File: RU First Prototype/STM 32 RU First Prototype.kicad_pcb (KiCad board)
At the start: 4 copper layers, 45 x 81.5 mm, 98 parts, among them J1 Conn_01x02, J10 Conn_01x02_Pin, J11 Conn_01x02_Pin, J12 1776113-2, J2 USB_C_Receptacle, J3 Conn_01x02_Pin, J4 Conn_01x04, J5 Conn_01x02_Pin, J7 1776113-2, J9 Conn_01x02_Pin, Q1 SISA96DN-T1, Q3 SISA96DN-T1, SW1 SW_SPDT, U1 STM32F412RGTx, U2 AMS1117-3.3, U3 MS5611, U4 KX134-1211, U5 W25Q16JVSS, U6 TCAN330, U7 TCAN330, Y1 Crystal_8Mhz

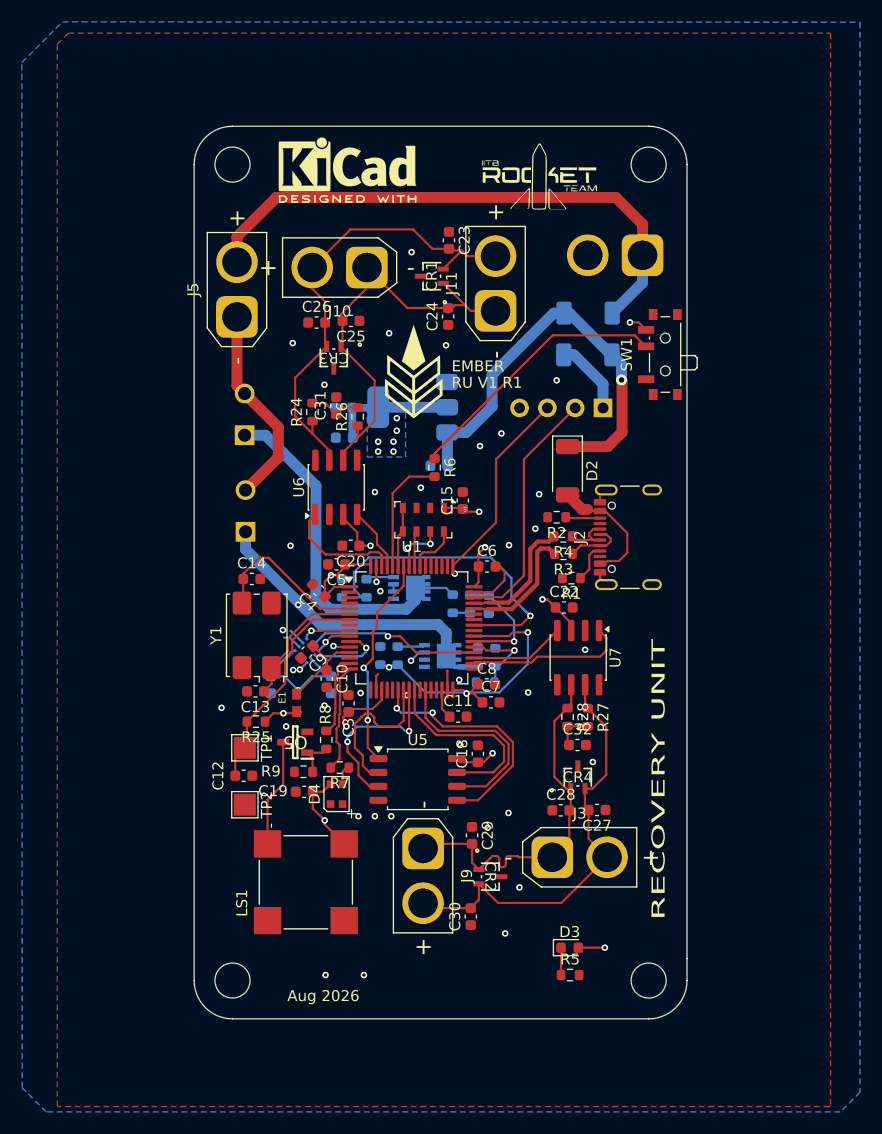
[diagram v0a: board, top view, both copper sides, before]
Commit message: changed CAN xt30 to jst 2.5
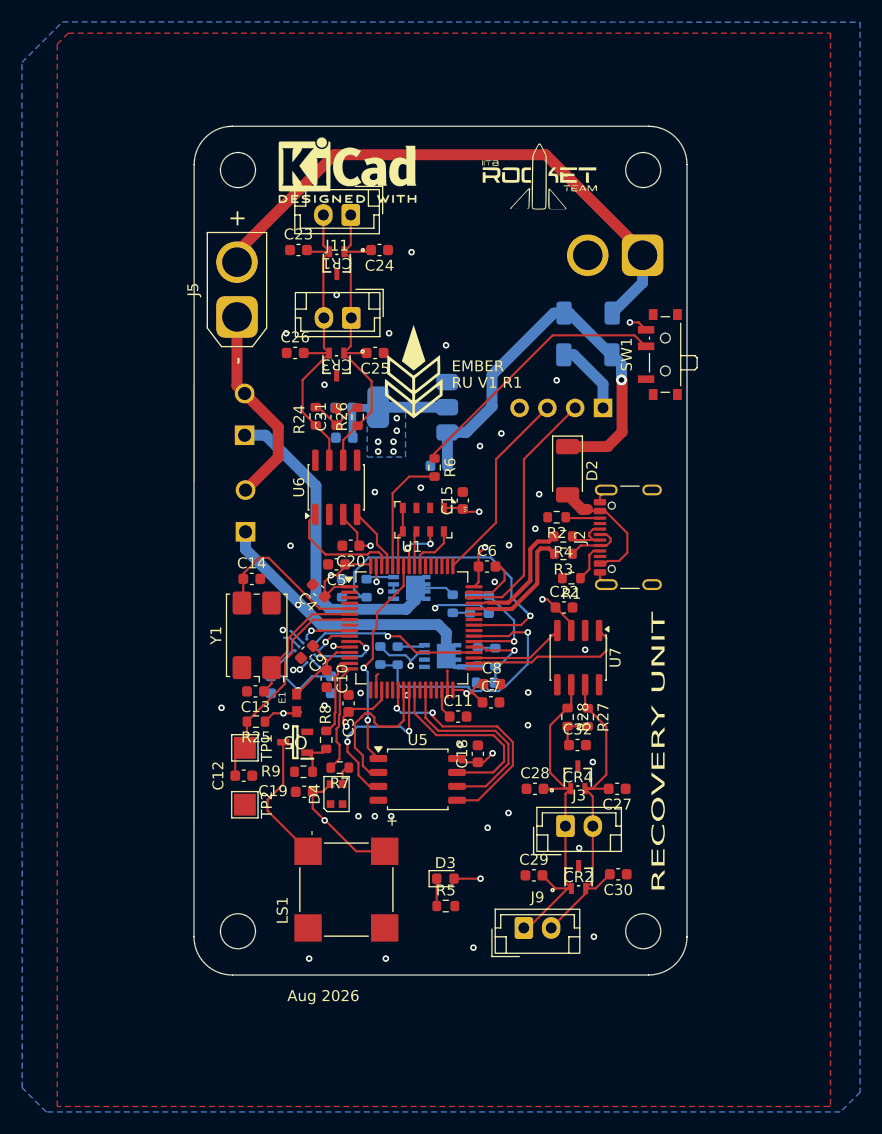
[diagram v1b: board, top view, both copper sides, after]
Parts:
- J10, J11, J3, J9: footprint Connector_AMASS:AMASS_XT30U-M_1x02_P5.0mm_Vertical -> Connector_JST:JST_EH_B2B-EH-A_1x02_P2.50mm_Vertical
- moved J11 15.9 mm to (115.8, 62.1), turned to 180 degrees
- moved C30 14.0 mm to (140.2, 122.3), turned to 180 degrees
- moved C23 13.8 mm to (111.0, 65.3), turned to 0 degrees
- moved D3 13.0 mm to (124.4, 122.7)
- moved R5 13.0 mm to (124.5, 125.2)
- moved J9 11.7 mm to (131.6, 127.2), turned to 0 degrees
- moved CR1 8.75 mm to (114.5, 66.5), turned to 180 degrees
- moved C24 8.72 mm to (118.4, 65.3), turned to 180 degrees
- moved CR2 8.06 mm to (136.6, 122.5), turned to 0 degrees
- moved C29 6.73 mm to (132.5, 122.4), turned to 0 degrees
- moved J10 4.82 mm to (115.8, 71.5)
- moved REF** 4.53 mm to (105.5, 127.5)
- moved REF** 4.53 mm to (142.5, 127.5)
- moved LS1 3.76 mm to (115.4, 123.7)
- moved C25 3.67 mm to (118.0, 74.7)
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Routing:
- net /CAN_H: track 43.7 -> 29.6 mm
- net GND: track 20.8 -> 30.4 mm, vias 44 -> 46
- net /CAN_L: track 39.2 -> 30.0 mm
- net /CAN_H2: track 40.1 -> 31.1 mm
- net +3V3: track 79.5 -> 83.2 mm
- net Net-(Q5-D): track 9.88 -> 12.1 mm
- net /CAN_L2: track 34.4 -> 32.4 mm
- net /Drogue: track 23.7 -> 25.2 mm
- net /V_2S: track 52.2 -> 53.1 mm
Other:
- board size 45 x 81.5 mm -> 45 x 77.5 mm

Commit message: edge cuts adjustments
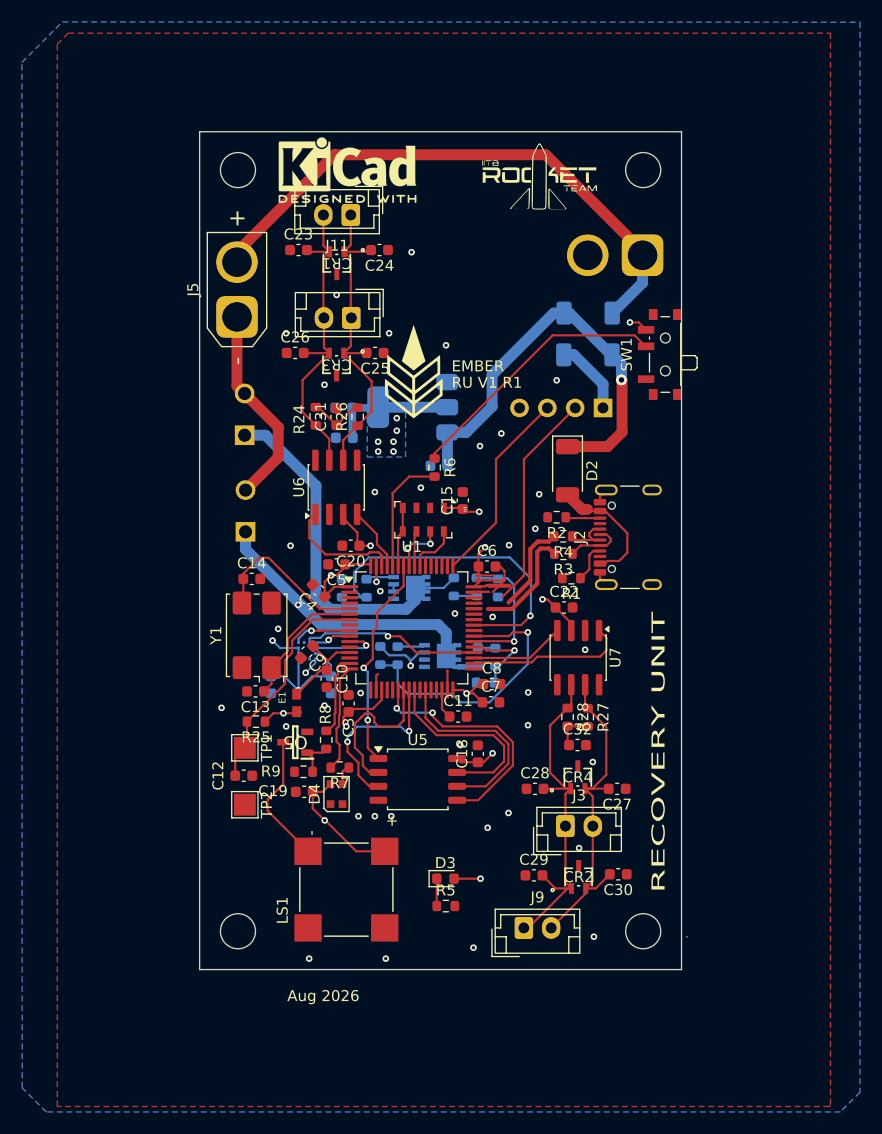
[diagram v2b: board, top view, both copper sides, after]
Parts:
- moved R20 1.74 mm to (129.2, 96.2)
- moved R19 1.68 mm to (127.3, 96.1)
- moved R18 1.54 mm to (125.2, 96.1)
- turned U4 to 180 degrees
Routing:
- net GND: track 30.4 -> 25.4 mm, vias 46 -> 44
- net /PC7: track 10.6 -> 12.7 mm
- net /D-: track 11.5 -> 10.3 mm
- net /KX_CS: track 4.43 -> 5.33 mm
- net /KX_SDI: track 7.34 -> 6.80 mm
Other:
- board size 45 x 77.5 mm -> 44.5 x 76.5 mm

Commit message: Final touch done from my side
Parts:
- removed the G*** at (121.5, 76.5)
- added G***: LOGO, RT_Graphics:project_logo_huge.kicad_sym, F.Cu at (110.0, 104.2)
- C15, U3: moved to B.Cu
- C16, C17, J1, U4: moved to F.Cu
- moved C15 25.4 mm to (109.3, 107.3), turned to -90 degrees
- moved C17 21.4 mm to (121.2, 87.8), turned to 90 degrees
- moved C16 18.8 mm to (123.9, 89.0), turned to 90 degrees
- moved U3 16.8 mm to (111.7, 102.9), turned to 0 degrees
- moved U4 14.8 mm to (121.5, 90.7)
- moved G*** 13.4 mm to (126.3, 70.6)
- moved REF** 10.5 mm to (126.0, 59.0)
- moved J1 9.70 mm to (135.5, 59.0), turned to -90 degrees
- moved TP2 2.19 mm to (106.1, 118.1)
- moved C12 1.95 mm to (106.1, 115.2)
- moved TP1 1.26 mm to (106.2, 112.0)
- moved REF** 0.71 mm to (106.0, 127.0)
- moved C19 0.70 mm to (111.5, 115.5)
- moved J5 0.59 mm to (106.0, 71.4)
- moved REF** 0.57 mm to (105.9, 58.4)
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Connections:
- U1 pad 10: /KX_SDO -> /ALT_SDO
- U1 pad 11: /KX_SDI -> /ALT_SDI
- U1 pad 36: /KX_SCK -> /ALT_SCLK
- U1 pad 55: /ALT_SCLK -> /KX_SCK
- U1 pad 56: /ALT_SDO -> /KX_SDO
- U1 pad 57: /ALT_SDI -> /KX_SDI
- U1 pad 59: /ALT_CS -> /KX_CS
- U1 pad 9: /KX_CS -> /ALT_CS
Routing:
- net /KX_SCK: track 16.3 -> 2.89 mm, vias 1 -> 0
- net /ALT_SCLK: track 4.66 -> 16.7 mm, vias 0 -> 1
- net +3V3: track 83.7 -> 77.3 mm
- net /ALT_SDI: track 5.04 -> 10.7 mm, vias 2 -> 1
- net GND: track 25.4 -> 29.5 mm, vias 44 -> 48
- net /V_2S: track 53.1 -> 49.5 mm
- net /ALT_CS: track 5.45 -> 7.21 mm, vias 0 -> 1
- net /KX_SDO: track 3.45 -> 5.20 mm, vias 1 -> 2
- net /BOOT0: track 11.1 -> 12.5 mm
- net /D-: track 10.3 -> 11.5 mm
- net /NRST: track 21.4 -> 22.4 mm
- net /KX_CS: track 5.33 -> 4.45 mm, vias 1 -> 0
- net /ALT_SDO: track 3.20 -> 3.99 mm, vias 0 -> 1
- net /Main: track 31.7 -> 31.0 mm
- net /V_USB: track 12.0 -> 11.5 mm
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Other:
- outline, holes or cut-outs redrawn
- board text added: "Every av component has to have a cursed looking prototype - The person who has this r*t**ded idead called TSMBAS"
- board text added: "REV 1"
- board text added: "RU V1R1"
- board text removed: "EMBER"
- board text removed: "RU V1 R1"

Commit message: Fixed schematic and some routing, flash routing left
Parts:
- moved C15 16.9 mm to (125.3, 112.8), turned to 0 degrees
- moved U3 11.8 mm to (120.9, 110.4), turned to 90 degrees
- moved E1 1.73 mm to (111.1, 104.9)
- moved R7 1.41 mm to (113.6, 113.3)
- moved C19 1.39 mm to (110.2, 115.8)
- moved C10 1.37 mm to (112.8, 103.3)
- moved C9 1.30 mm to (112.1, 100.7)
- moved R9 1.26 mm to (110.2, 113.1)
- moved D4 1.24 mm to (113.7, 115.9)
- moved Q5 0.90 mm to (109.8, 110.3)
- moved R25 0.80 mm to (106.8, 107.6)
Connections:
- U1 pad 1: +3V3 -> unconnected-(U1-VBAT-Pad1)
- U1 pad 10: /ALT_SDO -> unconnected-(U1-PC2-Pad10)
- U1 pad 11: /ALT_SDI -> unconnected-(U1-PC3-Pad11)
- U1 pad 14: unconnected-(U1-PA0-Pad14) -> /Buzzer_G
- U1 pad 15: /Buzzer_G -> /FLASH_IO3
- U1 pad 20: unconnected-(U1-PA4-Pad20) -> /ALT_CS
- U1 pad 21: unconnected-(U1-PA5-Pad21) -> /ALT_SCLK
- U1 pad 22: /FLASH_IO0 -> /ALT_SDI
- U1 pad 23: /FLASH_IO1 -> /ALT_SDO
- U1 pad 24: /FLASH_IO2 -> unconnected-(U1-PC4-Pad24)
- U1 pad 25: /FLASH_IO3 -> unconnected-(U1-PC5-Pad25)
- U1 pad 33: unconnected-(U1-PB12-Pad33) -> /CAN_RX2
- U1 pad 35: /CAN_RX2 -> unconnected-(U1-PB14-Pad35)
- U1 pad 36: /ALT_SCLK -> unconnected-(U1-PB15-Pad36)
- U1 pad 39: /Drogue -> /FLASH_IO2
- U1 pad 40: unconnected-(U1-PC9-Pad40) -> /FLASH_IO0
- U1 pad 42: unconnected-(U1-PA9-Pad42) -> /Drogue
- U1 pad 51: unconnected-(U1-PC10-Pad51) -> /FLASH_IO1
- U1 pad 52: unconnected-(U1-PC11-Pad52) -> /KX_SDI
- U1 pad 53: unconnected-(U1-PC12-Pad53) -> /KX_SDO
- U1 pad 56: /KX_SDO -> unconnected-(U1-PB4-Pad56)
- U1 pad 57: /KX_SDI -> unconnected-(U1-PB5-Pad57)
- U1 pad 9: /ALT_CS -> unconnected-(U1-PC1-Pad9)
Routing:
- net /FLASH_IO3: track 17.7 -> 0.00 mm
- net /FLASH_IO1: track 14.5 -> 27.0 mm, vias 0 -> 2
- net /FLASH_IO2: track 16.3 -> 27.8 mm
- net GND: track 29.5 -> 18.6 mm, vias 48 -> 43
- net /ALT_SCLK: track 16.7 -> 8.86 mm
- net /ALT_SDI: track 10.7 -> 4.46 mm
- net /CAN_TX2: track 14.7 -> 18.7 mm
- net /FLASH_IO0: track 22.3 -> 25.1 mm
- net /KX_SDI: track 6.60 -> 3.90 mm, vias 2 -> 0
- net /FLASH_CLK: track 18.5 -> 16.1 mm
- net /KX_SDO: track 5.20 -> 3.08 mm, vias 2 -> 0
- net /Drogue: track 25.4 -> 27.3 mm
- net Net-(D4-DIN): track 1.68 -> 0.00 mm
- net +3V3: track 77.3 -> 75.9 mm
- net /FLASH_CS: track 19.7 -> 21.1 mm, vias 2 -> 1
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
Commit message: Added flash chip and CAN bus 2 connections
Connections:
- U1 pad 1: unconnected-(U1-VBAT-Pad1) -> +3V3
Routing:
- net /FLASH_IO3: track 0.00 -> 17.3 mm, vias 0 -> 2
- net /FLASH_CS: track 21.1 -> 27.3 mm, vias 1 -> 2
- net GND: track 18.6 -> 24.0 mm, vias 43 -> 41
- net /CAN_TX2: track 18.7 -> 14.1 mm, vias 0 -> 2
- net +3V3: track 75.9 -> 80.0 mm, vias 19 -> 18
- net /Drogue: track 27.3 -> 30.5 mm
- net /CAN_RX2: track 9.06 -> 11.3 mm, vias 0 -> 2
- net /FLASH_IO0: track 25.1 -> 23.1 mm, vias 2 -> 0
- net Net-(D4-DIN): track 0.00 -> 1.80 mm
- net /FLASH_IO1: track 27.0 -> 25.3 mm
- net /FLASH_IO2: track 27.8 -> 29.2 mm, vias 2 -> 0
- net /PC6: track 7.79 -> 6.75 mm

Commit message: Some small fixes
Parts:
- moved C3 0.42 mm to (115.2, 106.6)
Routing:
- net +3V3: track 80.0 -> 82.8 mm
- net GND: track 24.0 -> 26.0 mm, vias 41 -> 48
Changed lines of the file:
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@@
 	(footprint "Capacitor_SMD:C_0603_1608Metric"
 		(layer "F.Cu")
-		(at 115.6 106.7 90)
+		(at 115.19 106.62 90)
 		(descr "Capacitor SMD 0603 (1608 Metric), square (rectangular) end terminal, IPC-7351 nominal, (Body size source: IPC-SM-782 page 76, https://www.pcb-3d.com/wordpress/wp-content/uploads/ipc-sm-782a_amendment_1_and_2.pdf), generated with kicad-footprint-generator")
 		(tags "capacitor")
@@
 	)
 	(segment
+		(start 115.7 101.55)
+		(end 117.56 101.55)
+		(width 0.2)
+		(layer "F.Cu")
+		(net "GND")
+	)
+	(segment
 		(start 125.65 96.55)
 		(end 127.05 96.55)
@@
 	)
 	(segment
+		(start 117.56 101.55)
+		(end 117.7 101.69)
+		(width 0.2)
+		(layer "F.Cu")
+		(net "GND")
+	)
+	(segment
 		(start 119.825 90.415)
 		(end 120.6975 90.415)
@@
 	)
 	(via
+		(at 142.95 99.43)
+		(size 0.6)
+		(drill 0.3)
+		(layers "F.Cu" "B.Cu")
+		(free yes)
+		(net "GND")
+	)
+	(via
 		(at 109.17 99.89)
 		(size 0.6)
@@
 	)
 	(via
+		(at 130.03 109.12)
+		(size 0.6)
+		(drill 0.3)
+		(layers "F.Cu" "B.Cu")
+		(free yes)
+		(net "GND")
+	)
+	(via
 		(at 125.4 99.82)
 		(size 0.6)
@@
 	)
 	(via
+		(at 117.13 102.31)
+		(size 0.6)
+		(drill 0.3)
+		(layers "F.Cu" "B.Cu")
+		(free yes)
+		(net "GND")
+	)
+	(via
 		(at 129.55 82.05)
 		(size 0.6)
@@
 	)
 	(via
+		(at 116.4 105.91)
+		(size 0.6)
+		(drill 0.3)
+		(layers "F.Cu" "B.Cu")
+		(free yes)
+		(net "GND")
+	)
+	(via
+		(at 133.27 97.05)
+		(size 0.6)
+		(drill 0.3)
+		(layers "F.Cu" "B.Cu")
+		(free yes)
+		(net "GND")
+	)
+	(via
 		(at 132.65 90.75)
 		(size 0.6)
@@
 	)
 	(via
+		(at 141.89 106.31)
+		(size 0.6)
+		(drill 0.3)
+		(layers "F.Cu" "B.Cu")
+		(free yes)
+		(net "GND")
+	)
+	(via
 		(at 125.8 110.5)
 		(size 0.6)
@@
 		(net "GND")
 	)
+	(via
+		(at 109.91 117.92)
+		(size 0.6)
+		(drill 0.3)
+		(layers "F.Cu" "B.Cu")
+		(free yes)
+		(net "GND")
+	)
 	(segment
 		(start 121.33 102.77)
@@
 	)
 	(segment
-		(start 115.13 107.945)
-		(end 115.6 107.475)
+		(start 125.225 122.7)
+		(end 127.65 122.7)
 		(width 0.2)
 		(layer "F.Cu")
@@
 	)
 	(segment
-		(start 125.225 122.7)
-		(end 127.65 122.7)
+		(start 113.14 115)
+		(end 111.815 115)
 		(width 0.2)
 		(layer "F.Cu")
@@
 	)
 	(segment
+		(start 118.625 106.28241)
+		(end 118.625 105.475)
+		(width 0.2)
+		(layer "F.Cu")
+		(net "+3V3")
+	)
+	(segment
 		(start 134.5 97.94)
 		(end 135.93 99.37)
@@
 	)
 	(segment
-		(start 115.14 108.83)
-		(end 115.14 108.54)
-		(width 0.2)
-		(layer "F.Cu")
-		(net "+3V3")
-	)
-	(segment
 		(start 126.37 105.78)
 		(end 126.62 105.78)
@@
 	)
 	(segment
-		(start 118.625 106.375)
-		(end 118.625 105.475)
-		(width 0.2)
-		(layer "F.Cu")
-		(net "+3V3")
-	)
-	(segment
 		(start 110.975 116.085)
 		(end 112.94 118.05)
@@
 	)
 	(segment
+		(start 115.19 107.395)
+		(end 117.51241 107.395)
+		(width 0.2)
+		(layer "F.Cu")
+		(net "+3V3")
+	)
+	(segment
 		(start 114 95)
 		(end 114.5 95)
@@
 	)
 	(segment
-		(start 115.875 107.2)
-		(end 117.8 107.2)
-		(width 0.2)
-		(layer "F.Cu")
-		(net "+3V3")
-	)
-	(segment
 		(start 125.125 105.475)
 		(end 126.065 105.475)
@@
 	)
 	(segment
-		(start 115.13 108.53)
-		(end 115.13 107.945)
-		(width 0.2)
-		(layer "F.Cu")
-		(net "+3V3")
-	)
-	(segment
 		(start 141.29 71.91)
 		(end 141.91 71.91)
@@
 	)
 	(segment
+		(start 117.51241 107.395)
+		(end 118.625 106.28241)
+		(width 0.2)
+		(layer "F.Cu")
+		(net "+3V3")
+	)
+	(segment
 		(start 120.6975 89.0925)
 		(end 121.19 88.6)
@@
 	)
 	(segment
-		(start 115.6 107.475)
-		(end 115.875 107.2)
-		(width 0.2)
-		(layer "F.Cu")
-		(net "+3V3")
-	)
-	(segment
 		(start 141.91 71.91)
 		(end 142.58 72.58)
@@
 	)
 	(segment
+		(start 111.815 115)
+		(end 110.975 115.84)
+		(width 0.2)
+		(layer "F.Cu")
+		(net "+3V3")
+	)
+	(segment
 		(start 126.37 105.78)
 		(end 127.005 105.78)
@@
 	)
 	(segment
-		(start 117.8 107.2)
-		(end 118.625 106.375)
+		(start 115.14 107.445)
+		(end 115.19 107.395)
 		(width 0.2)
 		(layer "F.Cu")
@@
 	)
 	(segment
-		(start 115.14 108.54)
-		(end 115.13 108.53)
+		(start 125.125 105.595)
+		(end 125.125 105.475)
 		(width 0.2)
 		(layer "F.Cu")
@@
 	)
 	(segment
-		(start 125.125 105.595)
-		(end 125.125 105.475)
+		(start 123.87 89.575)
+		(end 123.87 89.74)
 		(width 0.2)
 		(layer "F.Cu")
@@
 	)
 	(segment
-		(start 123.87 89.575)
-		(end 123.87 89.74)
+		(start 115.14 108.83)
+		(end 115.14 107.445)
 		(width 0.2)
 		(layer "F.Cu")
@@
 	)
 	(segment
+		(start 115.8 104.77)
+		(end 115.8 109.97)
+		(width 0.2)
+		(layer "B.Cu")
+		(net "/FLASH_IO1")
+	)
+	(segment
 		(start 118.79 100.18)
 		(end 117.16 100.18)
@@
 	(segment
 		(start 115.8 101.54)
-		(end 115.8 109.97)
+		(end 115.8 104.77)
 		(width 0.2)
 		(layer "B.Cu")
